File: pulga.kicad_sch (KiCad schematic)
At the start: 0 parts

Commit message: esquemático do conversor buck (~12V pra 3.3V)
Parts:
- added C1, C2, C3, C4, C5, C6: C, symbol Device:C
- added D1: D_Schottky, symbol Device:D_Schottky
- added L1: L, symbol Device:L
- added R1, R2, R3: R, symbol Device:R
- added U1: ~, Package_SO:SOIC-8_3.9x4.9mm_P1.27mm, symbol regulator_switch:TPS54331
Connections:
- new net: R2.2, R3.1, U1.4 (VSENSE)
- new net: C6.2, R3.2
- new net: C5.2, D1.1 (K), L1.1, U1.7 (PH)
- new net: R1.1, U1.5 (COMP)
- new net: C2.1, C3.1, C4.1, R1.2, U1.4 (VSENSE)
- new net: C6.1, L1.2, R2.1
- new net: C5.1, U1.1 (BOOT)
- new net 12V: C1.1, U1.2 (VIN)
- new net GND: C1.2, C2.2, C3.2, C4.2, D1.2 (A), U1.6 (GND)

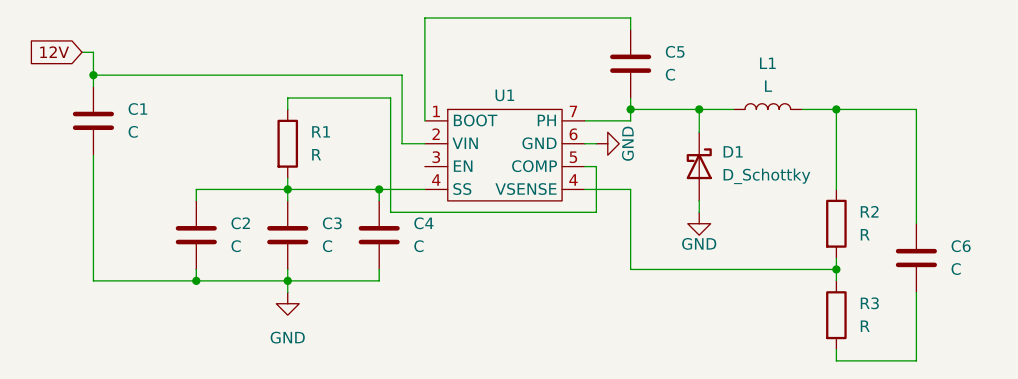
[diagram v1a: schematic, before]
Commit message: adicionando valor e footprint aos componentes do buck
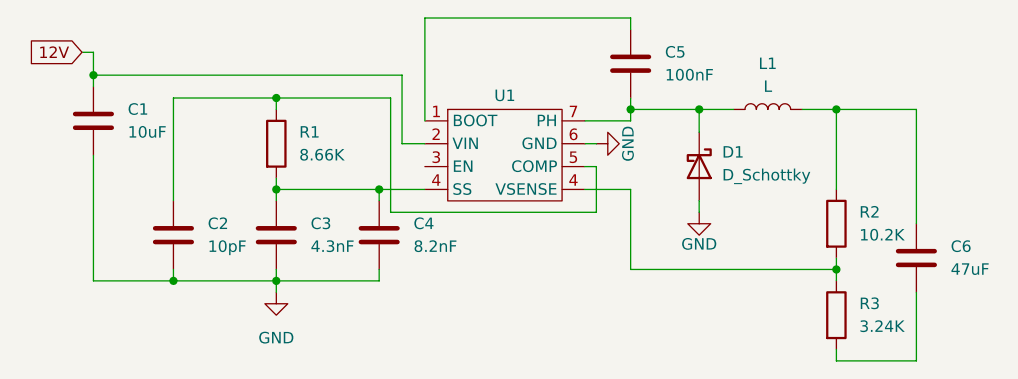
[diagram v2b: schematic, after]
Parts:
- C1: value C -> 10uF; footprint (none) -> Capacitor_SMD:C_1210_3225Metric
- C2: value C -> 10pF; footprint (none) -> Capacitor_SMD:C_0805_2012Metric
- C3: value C -> 4.3nF; footprint (none) -> Capacitor_SMD:C_0201_0603Metric
- C4: value C -> 8.2nF; footprint (none) -> Capacitor_SMD:C_0201_0603Metric
- C5: value C -> 100nF; footprint (none) -> Capacitor_SMD:C_0805_2012Metric
- C6: value C -> 47uF; footprint (none) -> Capacitor_SMD:C_1210_3225Metric
- D1: footprint (none) -> Diode_SMD:D_SMF
- L1: footprint (none) -> Inductor_SMD:L_Cenker_CKCS6045
- R1: value R -> 8.66K; footprint (none) -> Resistor_SMD:R_0402_1005Metric
- R2: value R -> 10.2K; footprint (none) -> Resistor_SMD:R_0402_1005Metric
- R3: value R -> 3.24K; footprint (none) -> Resistor_SMD:R_0402_1005Metric
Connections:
- net at R1.1, U1.5 (COMP): now also C2.1
- net at C3.1, C4.1, R1.2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: no longer C2.1
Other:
- moved on the sheet: C2, C3, R1

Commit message: correções no esquemático e ligação dos componentes do 54331 na pcb
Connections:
- net GND: now also C6.2, R3.2, U1.7 (GND); no longer U1.6 (GND)
- net at R2.2, R3.1: now also U1.5 (VSENSE); no longer U1.4 (VSENSE)
- net at C5.2, D1.1 (K), L1.1: now also U1.8 (PH); no longer U1.7 (PH)
- net at C2.1, R1.1: now also U1.6 (COMP); no longer U1.5 (COMP)
- net at C3.1, R1.2: no longer C4.1, U1.4 (VSENSE)
- new net: C4.1, U1.4 (SS)
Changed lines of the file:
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@@
+	)
+	(junction
+		(at 113.03 57.15)
+		(diameter 0)
+		(color 0 0 0 0)
 	)
 	(junction
@@
 	)
 	(junction
-		(at 41.91 38.1)
-		(diameter 0)
-		(color 0 0 0 0)
-	)
-	(junction
 		(at 104.14 46.99)
 		(diameter 0)
 		(color 0 0 0 0)
 	)
-	(junction
-		(at 53.34 38.1)
-		(diameter 0)
-		(color 0 0 0 0)
-	)
-	(wire
-		(pts
-			(xy 41.91 38.1) (xy 41.91 39.37)
+	(wire
+		(pts
+			(xy 41.91 36.83) (xy 41.91 39.37)
+		)
+		(stroke
+			(width 0)
+			(type default)
+		)
+	)
+	(wire
+		(pts
+			(xy 113.03 57.15) (xy 113.03 58.42)
 		)
 		(stroke
@@
 	(wire
 		(pts
-			(xy 41.91 38.1) (xy 53.34 38.1)
-		)
-		(stroke
-			(width 0)
-			(type default)
-		)
-	)
-	(wire
-		(pts
 			(xy 104.14 45.72) (xy 104.14 46.99)
 		)
@@
 		(pts
 			(xy 55.88 33.02) (xy 55.88 25.4)
-		)
-		(stroke
-			(width 0)
-			(type default)
-		)
-	)
-	(wire
-		(pts
-			(xy 41.91 36.83) (xy 41.91 38.1)
 		)
 		(stroke
@@
 		(pin "1"
 		)
-		(pin "4"
+		(pin "8"
 		)
 		(instances
@@
 					(unit 1)
 				)
+			)
+		)
+	)
+	(symbol
+		(lib_id "power:GND")
+		(at 113.03 58.42 0)
+		(unit 1)
+		(exclude_from_sim no)
+		(in_bom yes)
+		(on_board yes)
+		(dnp no)
+		(fields_autoplaced yes)
+		(property "Reference" "#PWR04"
+			(at 113.03 64.77 0)
+			(effects
+				(font
+					(size 1.27 1.27)
+				)
+				(hide yes)
+			)
+		)
+		(property "Value" "GND"
+			(at 113.03 63.5 0)
+			(effects
+				(font
+					(size 1.27 1.27)
+				)
+			)
+		)
+		(property "Footprint" ""
+			(at 113.03 58.42 0)
+			(effects
+				(font
+					(size 1.27 1.27)
+				)
+				(hide yes)
+			)
+		)
+		(property "Datasheet" ""
+			(at 113.03 58.42 0)
+			(effects
+				(font
+					(size 1.27 1.27)
+				)
+				(hide yes)
+			)
+		)
+		(property "Description" "Power symbol creates a global label with name \"GND\" , ground"
+			(at 113.03 58.42 0)
+			(effects
+				(font
+					(size 1.27 1.27)
+				)
+				(hide yes)
+			)
+		)
+		(pin "1"
+		)
+		(instances
+			(project ""
+				(path "/c94a0afd-57a6-467b-be84-ea3c3a5b4530"
+					(reference "#PWR04")
+					(unit 1)
+				)

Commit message: inserindo o esp32-c3 e reposicionando o circuito
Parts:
- added U2: ESP32-C3-WROOM-02, RF_Module:ESP32-C3-WROOM-02, symbol RF_Module:ESP32-C3-WROOM-02
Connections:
- net GND: now also U2.19 (GND), U2.9 (GND)
- net 3V3: now reaches C6.1, L1.2, R2.1
- net 3V3: now also U2.1 (3V3)

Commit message: adicionando o circuito do transceptor CAN (TCAN332GCDNR) no esquemático
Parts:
- added C10, C11, C12, C7, C8, C9: C, symbol Device:C
- added D2: NUP2105L, Package_TO_SOT_SMD:SOT-23, symbol Power_Protection:NUP2105L
- added R4, R5, R6, R7: R, symbol Device:R
- added U3: TCAN332G, Package_TO_SOT_SMD:SOT-23-8, symbol Interface_CAN_LIN:TCAN332G
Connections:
- net GND: now also C10.2, C11.1, C12.1, C8.2, C9.2, U3.2 (GND)
- net esp32_rx: now reaches U2.11 (IO20/RXD)
- net esp32_rx: now also R5.2
- net esp32_tx: now reaches U2.12 (IO21/TXD)
- net esp32_tx: now also R4.1
- new net: C7.2, D2.3 (A)
- new net: R6.1, U3.7 (CANH)
- new net: R7.1, U3.6 (CANL)
- new net: C10.1, R4.2, U3.1 (TXD)
- new net: R5.1, U3.4 (RXD)
- new net 3v3: C11.2, C12.2, U3.3 (VCC)
- new net can_h: C7.1, C8.1, C9.1, D2.1 (K), D2.2 (K), R6.2, R7.2

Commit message: ligando o circuito do CAN na PCB e corrigindo o esquemático
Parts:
- removed C7, C8, C9: C, symbol Device:C
- removed R6, R7: R, symbol Device:R
- C10, C11: value C -> 1u; footprint (none) -> Capacitor_SMD:C_0201_0603Metric
- C12: value C -> 100u; footprint (none) -> Capacitor_SMD:C_0201_0603Metric
- R4, R5: value R -> 1k; footprint (none) -> Resistor_SMD:R_0402_1005Metric
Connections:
- net 3v3 is gone; now on net 3V3: C11.2, C12.2, U3.3 (VCC)
- net GND: now also D2.3 (A)
- net can_h: now also U3.7 (CANH); no longer D2.2 (K)
- net can_l: now reaches U3.6 (CANL)
- net can_l: now also D2.2 (K)
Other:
- moved on the sheet: D2

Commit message: adicionando sistema de controle para o modo de boot do esp32
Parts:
- added C7: 100n, Capacitor_SMD:C_0201_0603Metric, symbol Device:C
- added R6, R7, R8, R9: 10k, Resistor_SMD:R_0201_0603Metric, symbol Device:R
- added SW1, SW2: SW_Push, Button_Switch_SMD:SW_SPST_B3U-1000P, symbol Switch:SW_Push
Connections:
- net 3V3: now also R6.1, R7.1, R8.1, R9.1
- net GND: now also SW1.1, SW2.2
- net at U2.16 (IO2): now also R7.2
- net chip_en: now reaches U2.2 (EN)
- net chip_en: now also C7.1, R8.2
- net at U2.7 (IO8): now also R6.2
- net boot: now reaches U2.8 (IO9)
- net boot: now also R9.2, SW2.1
- new net: C7.2, SW1.2
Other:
- moved on the sheet: U2

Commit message: adicionando o esquemático e footprint dos 4 pinos principais (12v, gnd, can_h e can_l) que vem do OBD
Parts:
- added J1: Conn_01x04_Pin, through_hole:obd_main_pins, symbol Connector:Conn_01x04_Pin
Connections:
- net 12V: now also J1.1 (Pin_1)
- net GND: now also J1.2 (Pin_2)
- net can_h: now also J1.3 (Pin_3)
- net can_l: now also J1.4 (Pin_4)
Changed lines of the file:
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@@
+	)
+	(junction
+		(at 21.59 48.26)
+		(diameter 0)
+		(color 0 0 0 0)
 	)
 	(junction
@@
 	(wire
 		(pts
+			(xy 130.81 116.84) (xy 134.62 116.84)
+		)
+		(stroke
+			(width 0)
+			(type default)
+		)
+	)
+	(wire
+		(pts
 			(xy 101.6 110.49) (xy 101.6 107.95)
 		)
@@
 	(wire
 		(pts
+			(xy 130.81 119.38) (xy 134.62 119.38)
+		)
+		(stroke
+			(width 0)
+			(type default)
+		)
+	)
+	(wire
+		(pts
 			(xy 41.91 27.94) (xy 30.48 27.94)
 		)
@@
 	(wire
 		(pts
+			(xy 20.32 48.26) (xy 21.59 48.26)
+		)
+		(stroke
+			(width 0)
+			(type default)
+		)
+	)
+	(wire
+		(pts
 			(xy 236.22 48.26) (xy 236.22 49.53)
 		)
@@
 	(wire
 		(pts
+			(xy 130.81 121.92) (xy 134.62 121.92)
+		)
+		(stroke
+			(width 0)
+			(type default)
+		)
+	)
+	(wire
+		(pts
 			(xy 58.42 30.48) (xy 58.42 19.05)
 		)
@@
 		(pts
 			(xy 20.32 22.86) (xy 21.59 22.86)
+		)
+		(stroke
+			(width 0)
+			(type default)
+		)
+	)
+	(wire
+		(pts
+			(xy 130.81 114.3) (xy 134.62 114.3)
 		)
 		(stroke
@@
 		)
 	)
+	(global_label "GND"
+		(shape input)
+		(at 134.62 116.84 0)
+		(fields_autoplaced yes)
+		(effects
+			(font
+				(size 1.27 1.27)
+			)
+			(justify left)
+		)
+		(property "Intersheetrefs" "${INTERSHEET_REFS}"
+			(at 141.4757 116.84 0)
+			(effects
+				(font
+					(size 1.27 1.27)
+				)
+				(justify left)
+				(hide yes)
+			)
+		)
+	)
+	(global_label "can_h"
+		(shape input)
+		(at 134.62 119.38 0)
+		(fields_autoplaced yes)
+		(effects
+			(font
+				(size 1.27 1.27)
+			)
+			(justify left)
+		)
+		(property "Intersheetrefs" "${INTERSHEET_REFS}"
+			(at 143.1084 119.38 0)
+			(effects
+				(font
+					(size 1.27 1.27)
+				)
+				(justify left)
+				(hide yes)
+			)
+		)
+	)
 	(global_label "3V3"
 		(shape input)
@@
 		)
 	)
+	(global_label "GND"
+		(shape input)
+		(at 20.32 48.26 180)
+		(fields_autoplaced yes)
+		(effects
+			(font
+				(size 1.27 1.27)
+			)
+			(justify right)
+		)
+		(property "Intersheetrefs" "${INTERSHEET_REFS}"
+			(at 13.4643 48.26 0)
+			(effects
+				(font
+					(size 1.27 1.27)
+				)
+				(justify right)
+				(hide yes)
+			)
+		)
+	)
 	(global_label "3V3"
 		(shape input)
@@
 		)
 	)
+	(global_label "can_l"
+		(shape input)
+		(at 134.62 121.92 0)
+		(fields_autoplaced yes)
+		(effects
+			(font
+				(size 1.27 1.27)
+			)
+			(justify left)
+		)
+		(property "Intersheetrefs" "${INTERSHEET_REFS}"
+			(at 142.6246 121.92 0)
+			(effects
+				(font
+					(size 1.27 1.27)
+				)
+				(justify left)
+				(hide yes)
+			)
+		)
+	)
 	(global_label "3V3"
 		(shape input)
@@
 		(property "Intersheetrefs" "${INTERSHEET_REFS}"
 			(at 112.6284 110.49 0)
+			(effects
+				(font
+					(size 1.27 1.27)
+				)
+				(justify left)
+				(hide yes)
+			)
+		)
+	)
+	(global_label "12V"
+		(shape input)
+		(at 134.62 114.3 0)
+		(fields_autoplaced yes)
+		(effects
+			(font
+				(size 1.27 1.27)
+			)
+			(justify left)
+		)
+		(property "Intersheetrefs" "${INTERSHEET_REFS}"
+			(at 141.1128 114.3 0)
 			(effects
 				(font
@@
 					(unit 1)
 				)
+			)
+		)
+	)
+	(symbol
+		(lib_id "Connector:Conn_01x04_Pin")
+		(at 125.73 116.84 0)
+		(unit 1)
+		(exclude_from_sim no)
+		(in_bom yes)
+		(on_board yes)
+		(dnp no)
+		(fields_autoplaced yes)
+		(property "Reference" "J1"
+			(at 126.365 109.22 0)
+			(effects
+				(font
+					(size 1.27 1.27)
+				)
+			)
+		)
+		(property "Value" "Conn_01x04_Pin"
+			(at 126.365 111.76 0)
+			(effects
+				(font
+					(size 1.27 1.27)
+				)
+			)
+		)
+		(property "Footprint" "through_hole:obd_main_pins"
+			(at 125.73 116.84 0)
+			(effects
+				(font
+					(size 1.27 1.27)
+				)
+				(hide yes)
+			)
+		)
+		(property "Datasheet" "~"
+			(at 125.73 116.84 0)
+			(effects
+				(font
+					(size 1.27 1.27)
+				)
+				(hide yes)
+			)
+		)
+		(property "Description" "Generic connector, single row, 01x04, script generated"
+			(at 125.73 116.84 0)
+			(effects
+				(font
+					(size 1.27 1.27)
+				)
+				(hide yes)
+			)
+		)
+		(pin "3"
+		)
+		(pin "2"
+		)
+		(pin "1"
+		)
+		(pin "4"
+		)
+		(instances
+			(project ""
+				(path "/c94a0afd-57a6-467b-be84-ea3c3a5b4530"
+					(reference "J1")
+					(unit 1)
+				)
